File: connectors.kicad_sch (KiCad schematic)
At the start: 34 parts, among them J1 Molex_Nano-Fit_1x2_SMD_105430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, J2 Conn_FAKRA_59S2AQ-40MT5-Z_1, J3 Conn_FAKRA_59S2AQ-40MT5-Z_1, J4 Conn_FAKRA_59S2AQ-40MT5-Z_1, J5 Conn_FAKRA_59S2AQ-40MT5-Z_1, J6 Conn_FFC_WE_68715014522, U1 SN74LV1T125DBVR, U2 SN74LV1T125DBVR

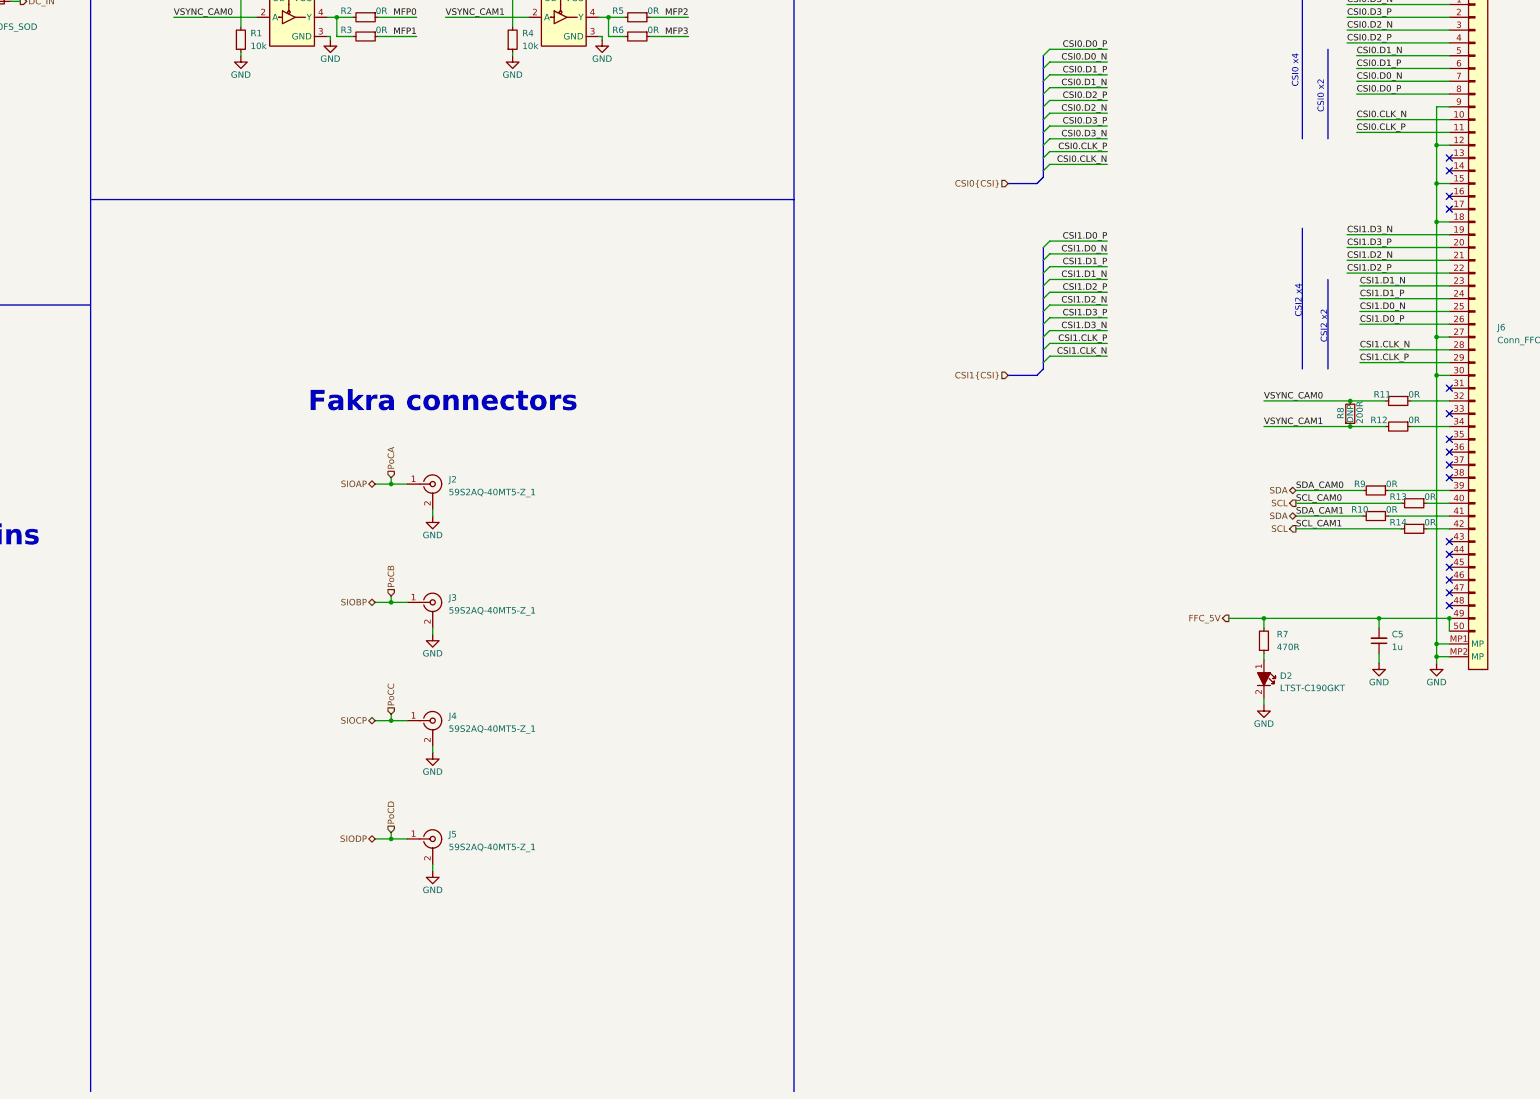
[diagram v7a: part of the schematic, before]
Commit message: Connectors: add buffer gates for I2C
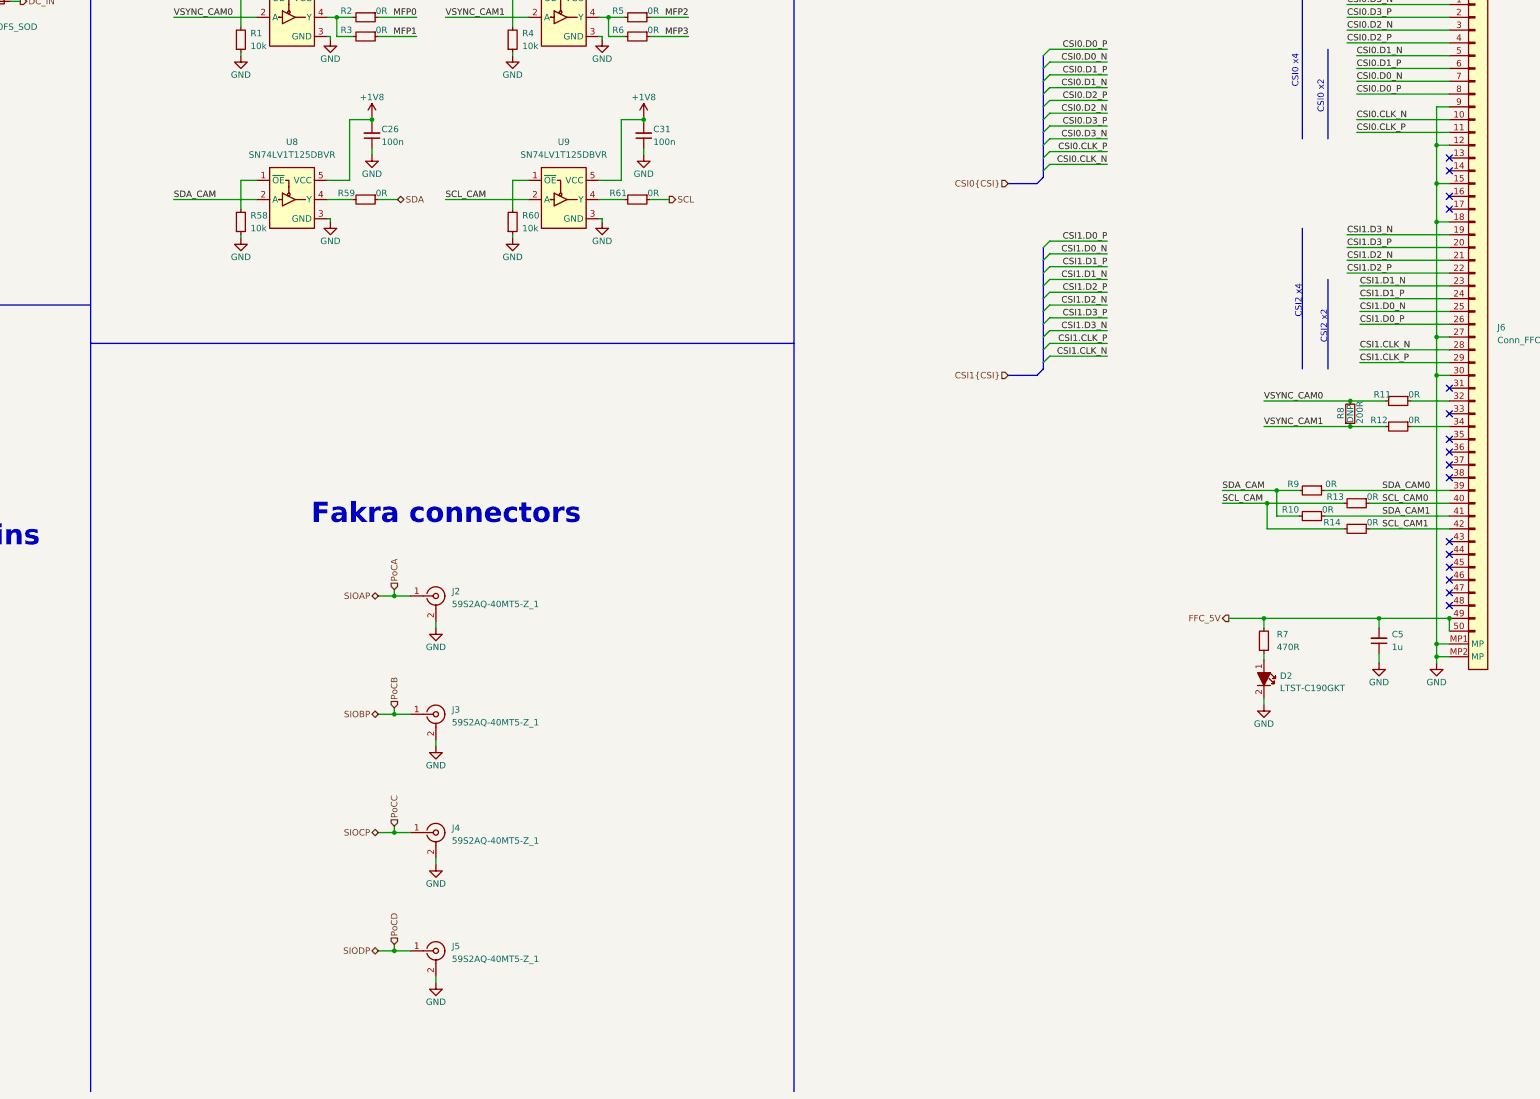
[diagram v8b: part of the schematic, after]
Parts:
- added C26, C31: C_100n_0402, antmicro-footprints:C_0402_1005Metric, symbol antmicroCapacitors0402:C_100n_0402
- added R58, R60: R_10k_0402, antmicro-footprints:R_0402_1005Metric, symbol antmicroResistors0402:R_10k_0402
- added R59, R61: R_0R_0402, antmicro-footprints:R_0402_1005Metric, symbol antmicroResistors0402:R_0R_0402
- added U8, U9: SN74LV1T125DBVR, antmicro-footprints:SOT-23-5, symbol antmicroLogicBuffersDriversReceiversTransceivers:SN74LV1T125DBVR
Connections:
- net +1V8: now also C26.2, C31.2, U8.5 (VCC), U9.5 (VCC)
- net GND: now also C26.1, C31.1, R58.1, R60.1, U8.3 (GND), U9.3 (GND)
- net SCL: now also R61.1; no longer R13.2, R14.2
- net SDA: now also R59.1; no longer R10.2, R9.2
- net SDA_CAM0: now reaches J6.39, R9.1
- net SDA_CAM1: now reaches J6.41, R10.1
- net SCL_CAM0: now reaches J6.40, R13.1
- net SCL_CAM1: now reaches J6.42, R14.1
- new net: R58.2, U8.1 (~{OE})
- new net: R59.2, U8.4 (Y)
- new net: R61.2, U9.4 (Y)
- new net: R60.2, U9.1 (~{OE})
- new net SCL_CAM: R13.2, R14.2, U9.2 (A)
- new net SDA_CAM: R10.2, R9.2, U8.2 (A)
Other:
- moved on the sheet: J2, J3, J4, J5, R10, R13, R14, R9
